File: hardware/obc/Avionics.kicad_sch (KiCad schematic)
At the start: 42 parts, among them J1 Conn_02x20_Odd_Even, J10 Conn_01x04, J15 Conn_01x02, J8 Conn_01x09, J9 Conn_01x03, U1 MAX706RESA, U2 ATSAMD51J20A-AU, Y1 32.768kHz

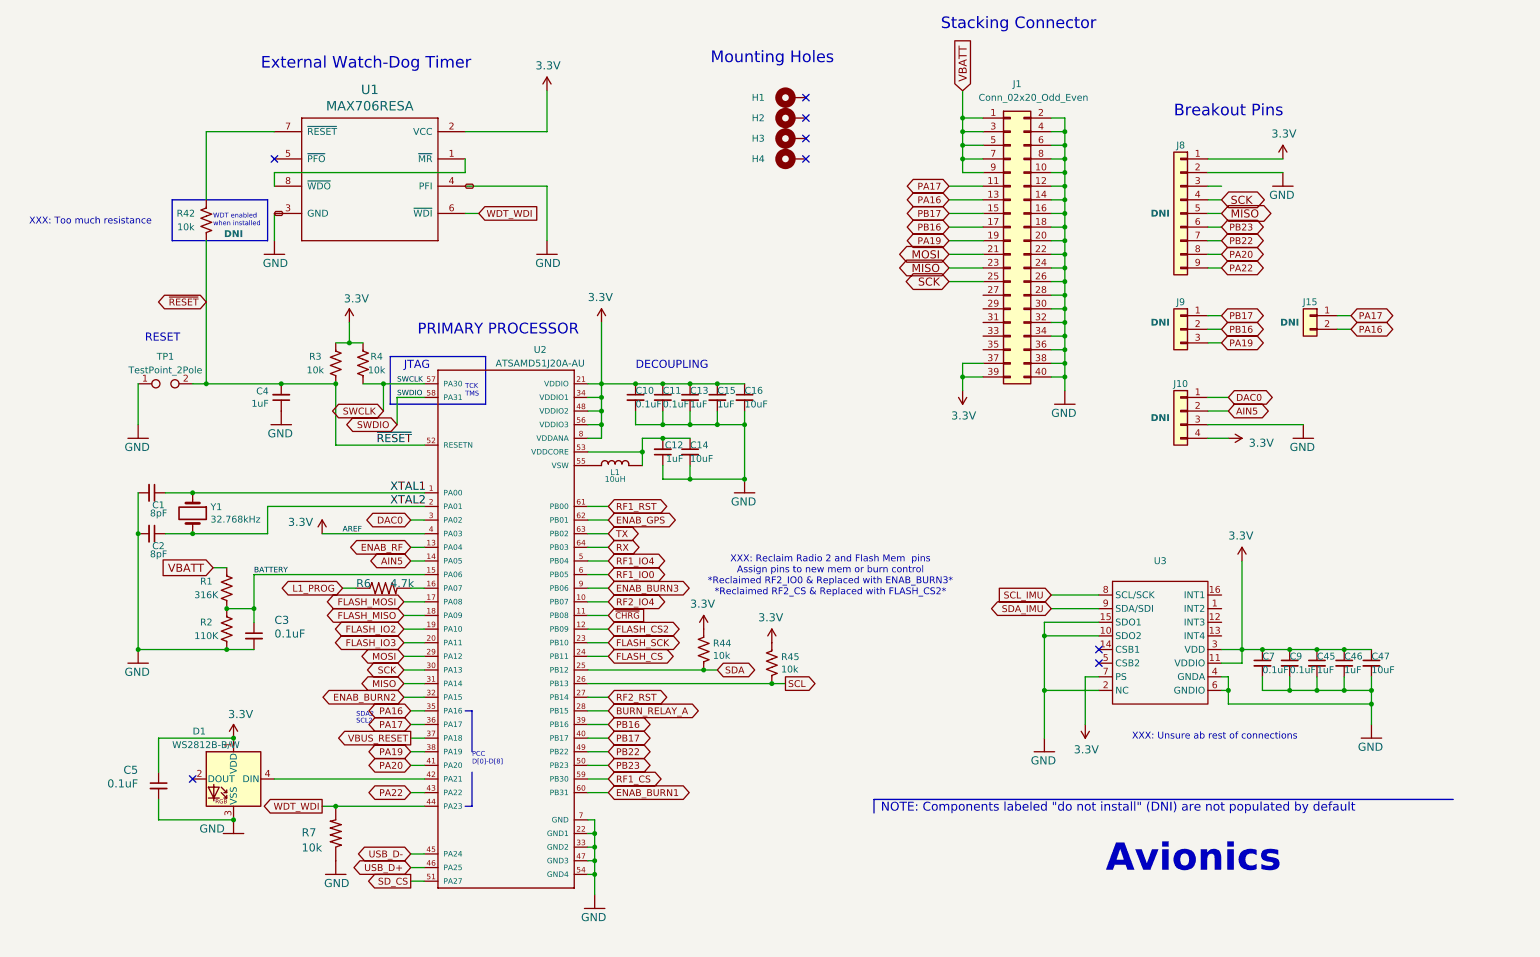
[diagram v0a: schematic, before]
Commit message: obc: Schematic pages to US Letter (except Power)
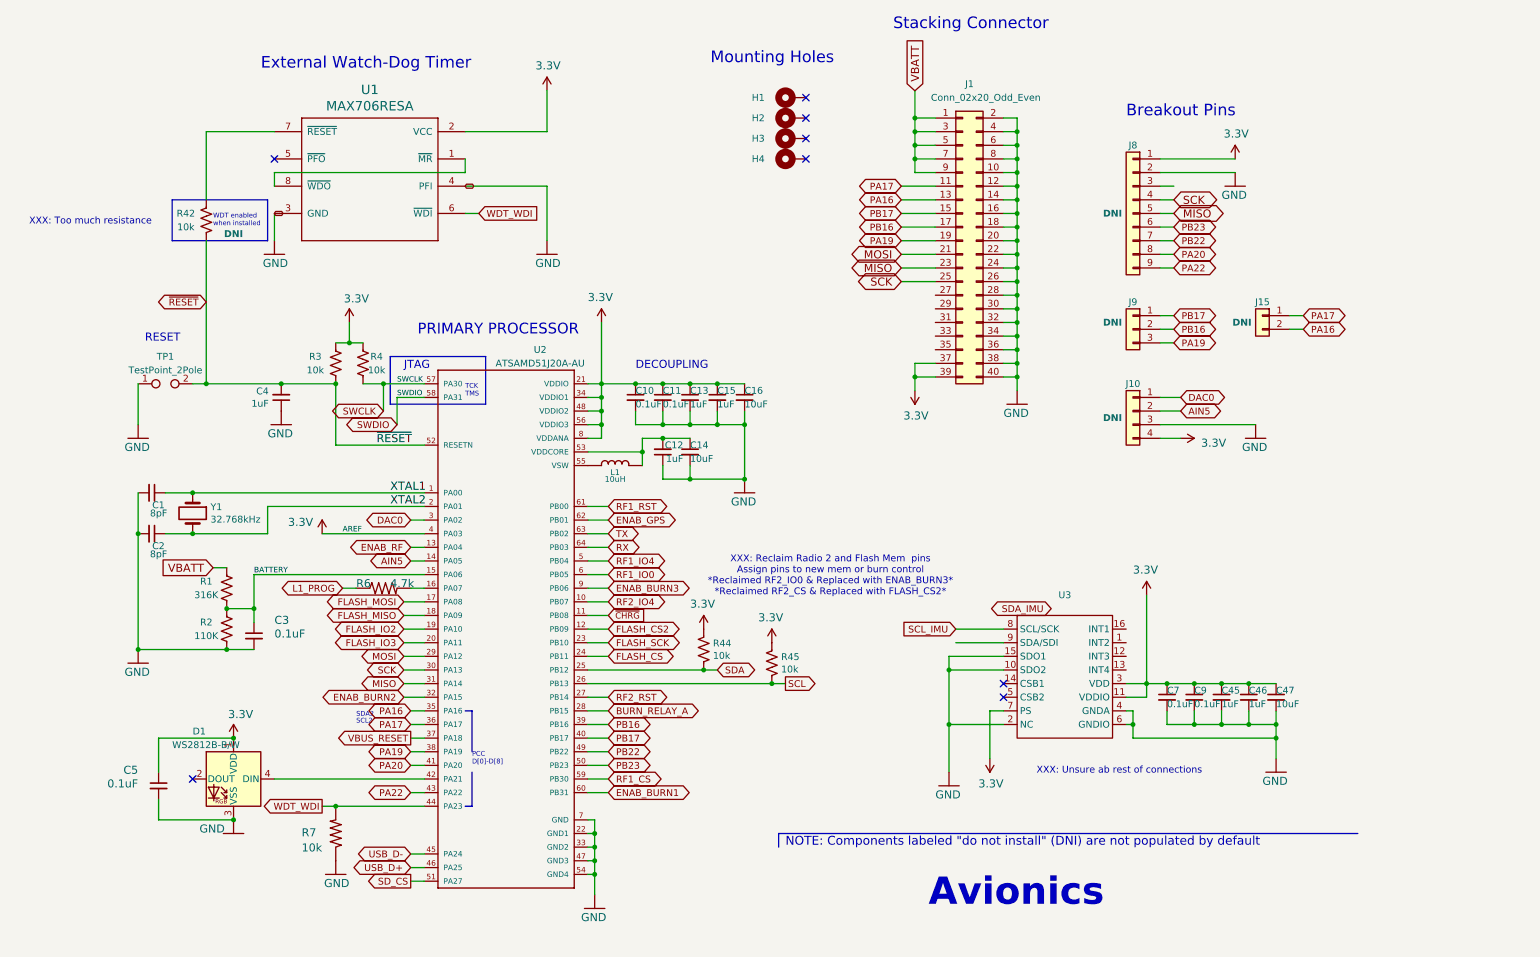
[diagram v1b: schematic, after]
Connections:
- net SDA_IMU: no longer U3.9 (SDA/SDI)
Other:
- moved on the sheet: C45, C46, C47, C7, C9, J1, J10, J15, J8, J9, U3

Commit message: obc: Add many XXX comments documenting 5/3 review
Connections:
- net SDA_IMU: now also U3.9 (SDA/SDI)
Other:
- note added: "XXX - do the JTAG signals (TCK/SWCLK, TMS/SWDIO) go anywhere? They should go to at least a pin header with GND, 3V3, and those two signals, that we can use for debugging."
- note added: "XXX identify which of these pins go elsewhere in the design. Those that don't, remove hierarchal connector and add no-connect (X)"
- note added: "XXX if these connectors on the right are obsoleted, remove"
- note added: "XXX make these hierarchal connectors the same size / not look wonky"
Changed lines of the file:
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@@
+		)
+	)
+	(text "XXX identify which of these pins go elsewhere in the design.\nThose that don't, remove hierarchal connector and add\nno-connect (X)"
+		(exclude_from_sim no)
+		(at 175.26 112.014 0)
+		(effects
+			(font
+				(size 1.27 1.27)
+			)
 		)
 	)
@@
 		)
 	)
+	(text "XXX - do the JTAG signals (TCK/SWCLK, TMS/SWDIO) go\nanywhere?  They should go to at least a pin header\nwith GND, 3V3, and those two signals, that we can use\nfor debugging."
+		(exclude_from_sim no)
+		(at 90.424 64.516 0)
+		(effects
+			(font
+				(size 1 1)
+			)
+		)
+	)
 	(text "NOTE: Components labeled \"do not install\" (DNI) are not populated by default"
 		(exclude_from_sim no)
@@
 			)
 			(justify left bottom)
+		)
+	)
+	(text "XXX make these hierarchal connectors\nthe same size / not look wonky"
+		(exclude_from_sim no)
+		(at 158.496 71.628 0)
+		(effects
+			(font
+				(size 1.27 1.27)
+			)
 		)
 	)
@@
 		)
 	)
+	(text "XXX if these connectors on the right\nare obsoleted, remove"
+		(exclude_from_sim no)
+		(at 238.76 103.632 0)
+		(effects
+			(font
+				(size 1.27 1.27)
+			)
+		)
+	)
 	(label "XTAL1"
 		(at 86.36 105.41 0)
@@
 	(global_label "SDA_IMU"
 		(shape bidirectional)
-		(at 209.55 127 180)
-		(effects
-			(font
-				(size 1.27 1.27)
-			)
-			(justify right)
-		)
-		(property "Intersheetrefs" "${INTERSHEET_REFS}"
-			(at 209.55 127 0)
-			(effects
-				(font
+		(at 191.77 133.35 180)
+		(effects
+			(font
+				(size 1.27 1.27)
+			)
+			(justify right)
+		)
+		(property "Intersheetrefs" "${INTERSHEET_REFS}"
+			(at 191.77 133.35 0)
+			(effects
+				(font

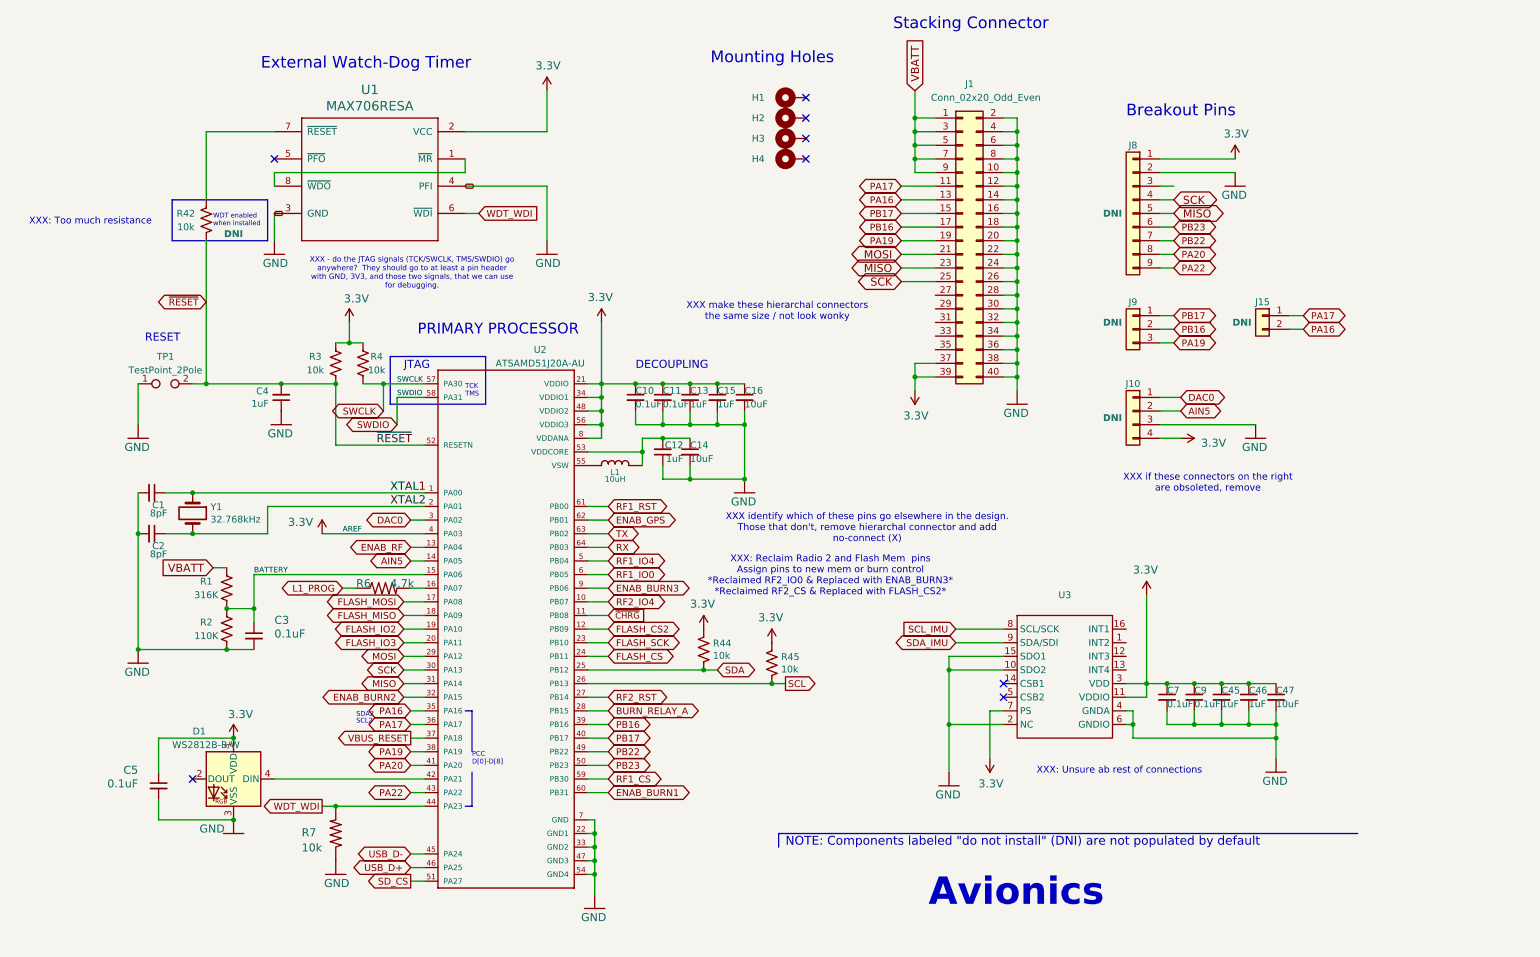
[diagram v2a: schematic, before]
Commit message: obc: schematic cleanup and wiring
Demarcated NC pins, added High-Rel connectors, cleaned up schematic legibility, and added bus protection for stacking signals SDA & SCL.
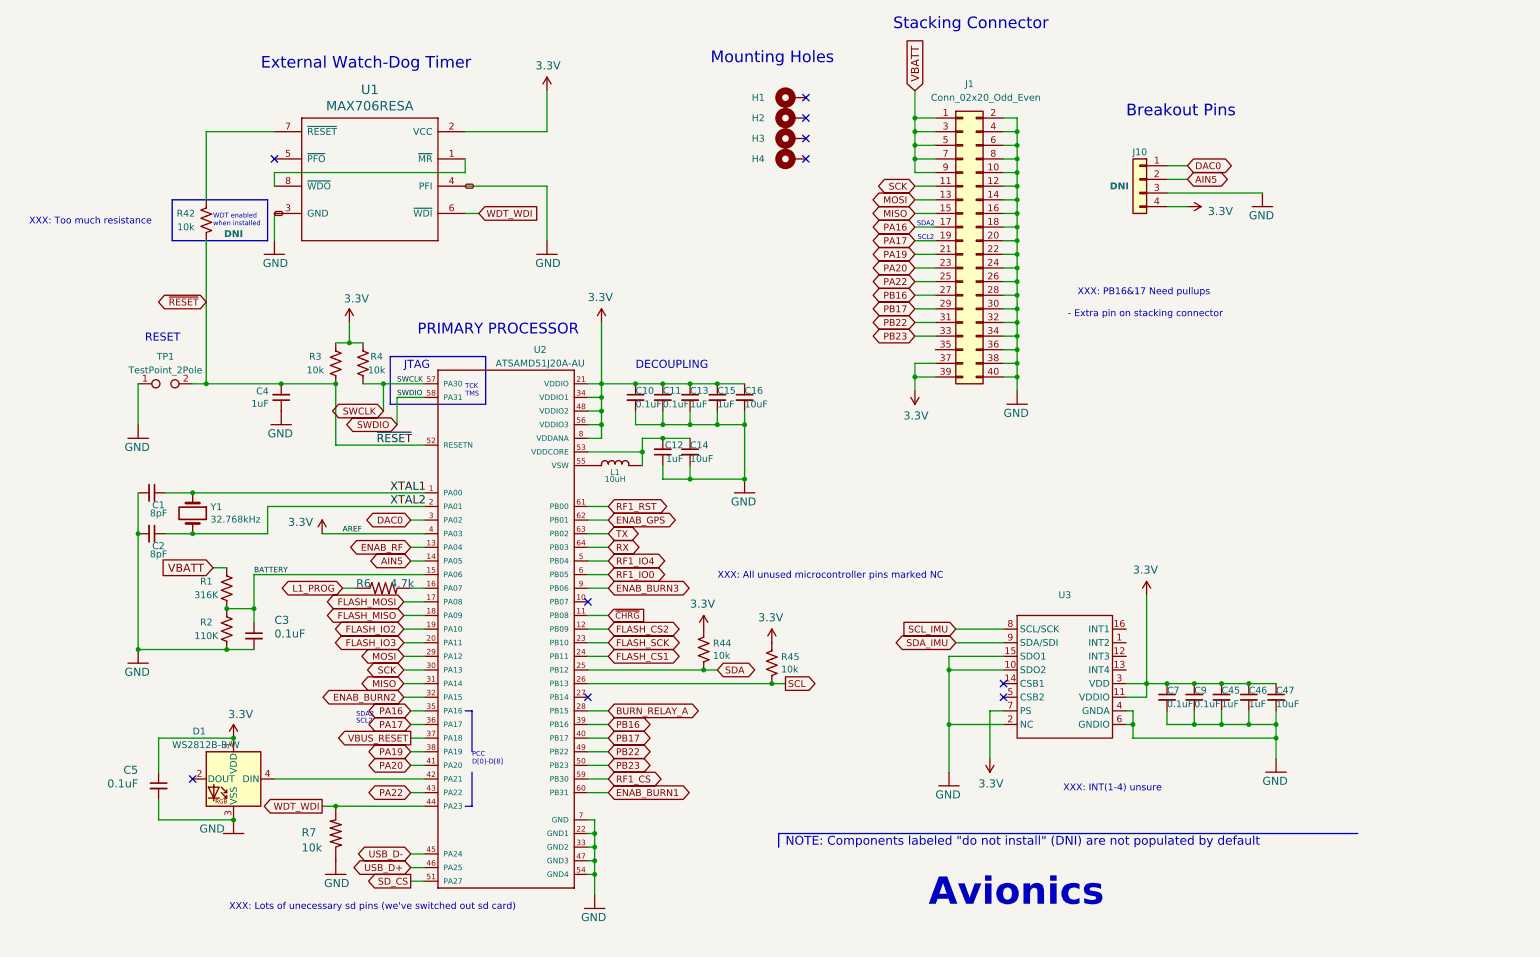
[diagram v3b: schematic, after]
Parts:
- removed J15: Conn_01x02, mainboard:PinHeader_CUSTOM3, symbol Connector_Generic:Conn_01x02
- removed J8: Conn_01x09, Connector_PinHeader_2.54mm:PinHeader_1x09_P2.54mm_Vertical, symbol Connector_Generic:Conn_01x09
- removed J9: Conn_01x03, Connector_PinHeader_2.54mm:PinHeader_1x03_P2.54mm_Vertical, symbol Connector_Generic:Conn_01x03
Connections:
- net MISO: now also J1.15 (Pin_15); no longer J1.23 (Pin_23)
- net MOSI: now also J1.13 (Pin_13); no longer J1.21 (Pin_21)
- net PA16: now also J1.17 (Pin_17); no longer J1.13 (Pin_13)
- net PA17: now also J1.19 (Pin_19); no longer J1.11 (Pin_11)
- net PA19: now also J1.21 (Pin_21); no longer J1.19 (Pin_19)
- net PA20: now also J1.23 (Pin_23)
- net PA22: now also J1.25 (Pin_25)
- net PB16: now also J1.27 (Pin_27); no longer J1.17 (Pin_17)
- net PB17: now also J1.29 (Pin_29); no longer J1.15 (Pin_15)
- net PB22: now also J1.31 (Pin_31)
- net PB23: now also J1.33 (Pin_33)
- net SCK: now also J1.11 (Pin_11); no longer J1.25 (Pin_25)
- net FLASH_CS renamed FLASH_CS1
- net RF2_IO4: no longer names the net of U2.10 (PB07)
- net RF2_RST: no longer names the net of U2.27 (PB14)
- no-connect marks 8 -> 10
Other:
- note added: "XXX: All unused microcontroller pins marked NC"
- note added: "XXX: INT(1-4) unsure"
- note added: "XXX: Lots of unecessary sd pins (we've switched out sd card)"
- note added: "XXX: PB16&17 Need pullups - Extra pin on stacking connector"
- note removed: "XXX - do the JTAG signals (TCK/SWCLK, TMS/SWDIO) go anywhere? They should go to at least a pin header with GND, 3V3, and those two signals, that we can use for debugging."
- note removed: "XXX identify which of these pins go elsewhere in the design. Those that don't, remove hierarchal connector and add no-connect (X)"
- note removed: "XXX if these connectors on the right are obsoleted, remove"
- note removed: "XXX make these hierarchal connectors the same size / not look wonky"
- note removed: "XXX: Reclaim Radio 2 and Flash Mem pins Assign pins to new mem or burn control *Reclaimed RF2_IO0 & Replaced with ENAB_BURN3* *Reclaimed RF2_CS & Replaced with FLASH_CS2*"
- note removed: "XXX: Unsure ab rest of connections"
- moved on the sheet: J10

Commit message: obc: schematic editing and footprint development
Deleted irrelevant SD-related circuits and pins. Created new & modified existing connector and inductor footprints. Added new components (Bat Charger, High-Rel Connector, etc.)
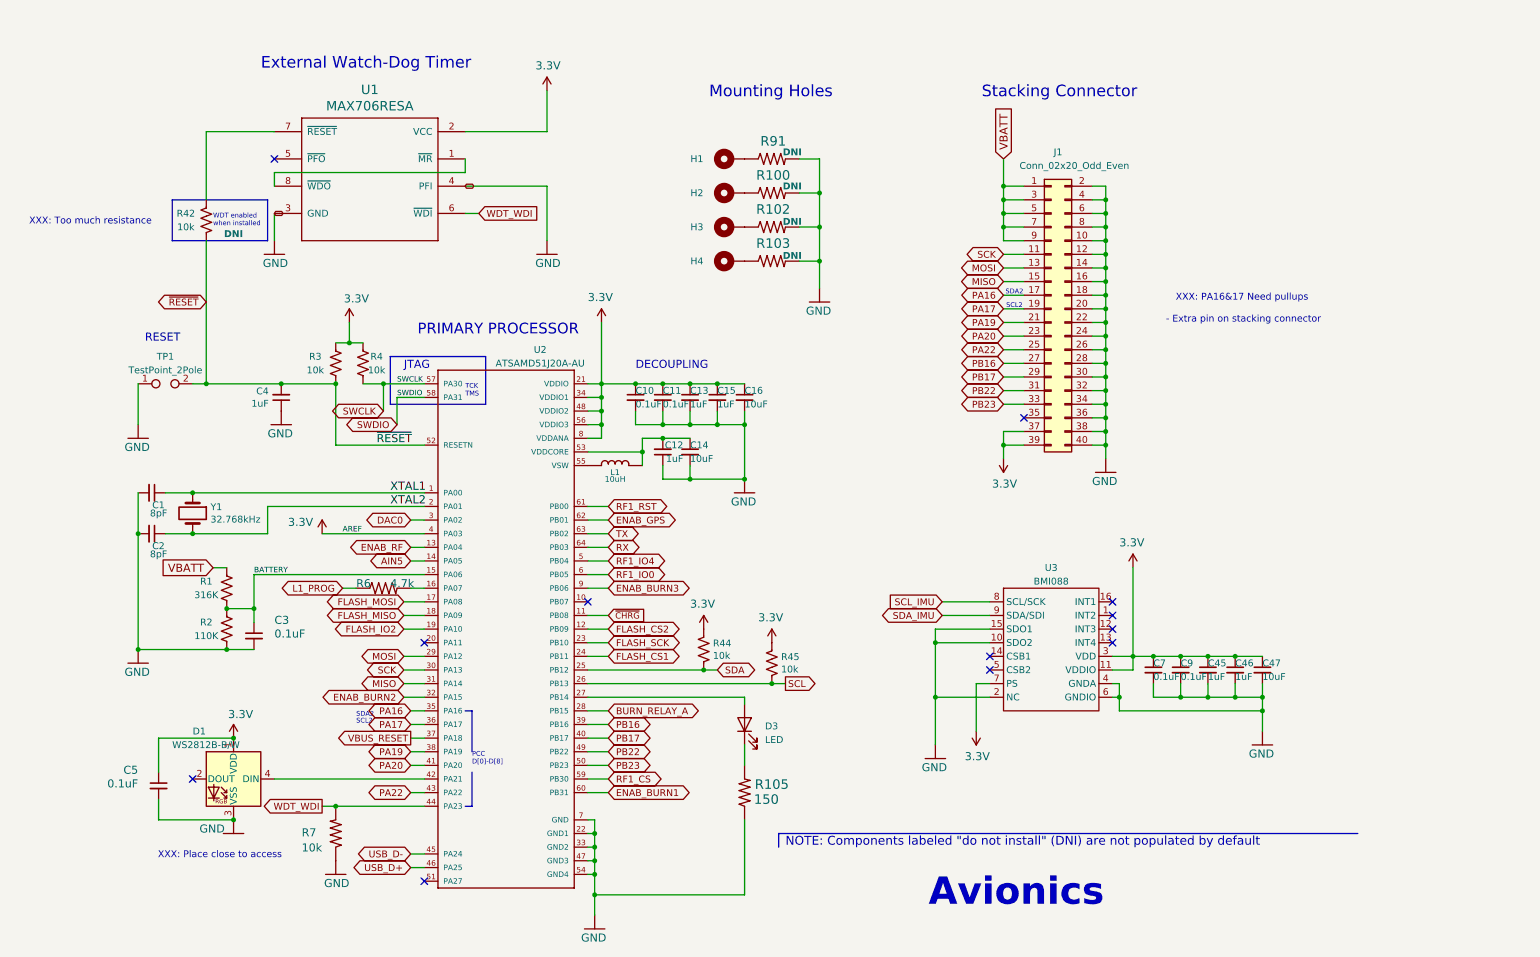
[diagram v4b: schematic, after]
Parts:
- removed J10: Conn_01x04, Connector_PinHeader_2.54mm:PinHeader_1x04_P2.54mm_Vertical, symbol Connector_Generic:Conn_01x04
- added D3: LED, LED_SMD:LED_0805_2012Metric, symbol Device:LED
- added R100, R102, R103, R91: NA, symbol mainboard:RESISTOR0603
- added R105: 150, Resistor_SMD:R_0603_1608Metric, symbol mainboard:RESISTOR0603
- L1: footprint Inductor_SMD:L_0805_2012Metric_Pad1.15x1.40mm_HandSolder -> SSE_Footprints:Sunlord_0805_2.0x1.6mm
- U3: value ~ -> BMI088; footprint (none) -> SSE_Footprints:LGA-16_4.5x3.0mm_P0.5mm; Manufacturer_Name (none) -> Bosch Sensortec; Manufacturer_Part_Number (none) -> BMI088
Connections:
- net GND: now also R100.2, R102.2, R103.2, R105.1, R91.2
- net at U2.27 (PB14): now also D3.2 (A)
- net at H1.1: now also R91.1
- net at H2.1: now also R100.1
- net at H3.1: now also R102.1
- net at H4.1: now also R103.1
- net FLASH_IO3: no longer names the net of U2.20 (PA11)
- net SD_CS: no longer names the net of U2.51 (PA27)
- new net: D3.1 (K), R105.2
- no-connect marks 10 -> 12
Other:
- note added: "XXX: PA16&17 Need pullups - Extra pin on stacking connector"
- note added: "XXX: Place close to access"
- note removed: "Breakout Pins"
- note removed: "XXX: All unused microcontroller pins marked NC"
- note removed: "XXX: INT(1-4) unsure"
- note removed: "XXX: Lots of unecessary sd pins (we've switched out sd card)"
- note removed: "XXX: PB16&17 Need pullups - Extra pin on stacking connector"
- moved on the sheet: C45, C46, C47, C7, C9, H1, H2, H3, H4, J1, U3
